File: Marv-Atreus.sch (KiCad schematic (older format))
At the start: 104 parts, among them SW1 SW_Push, U1 ATmega32U4-AU, U2 USBLC6-2SC6, Y1 Resonator_Small

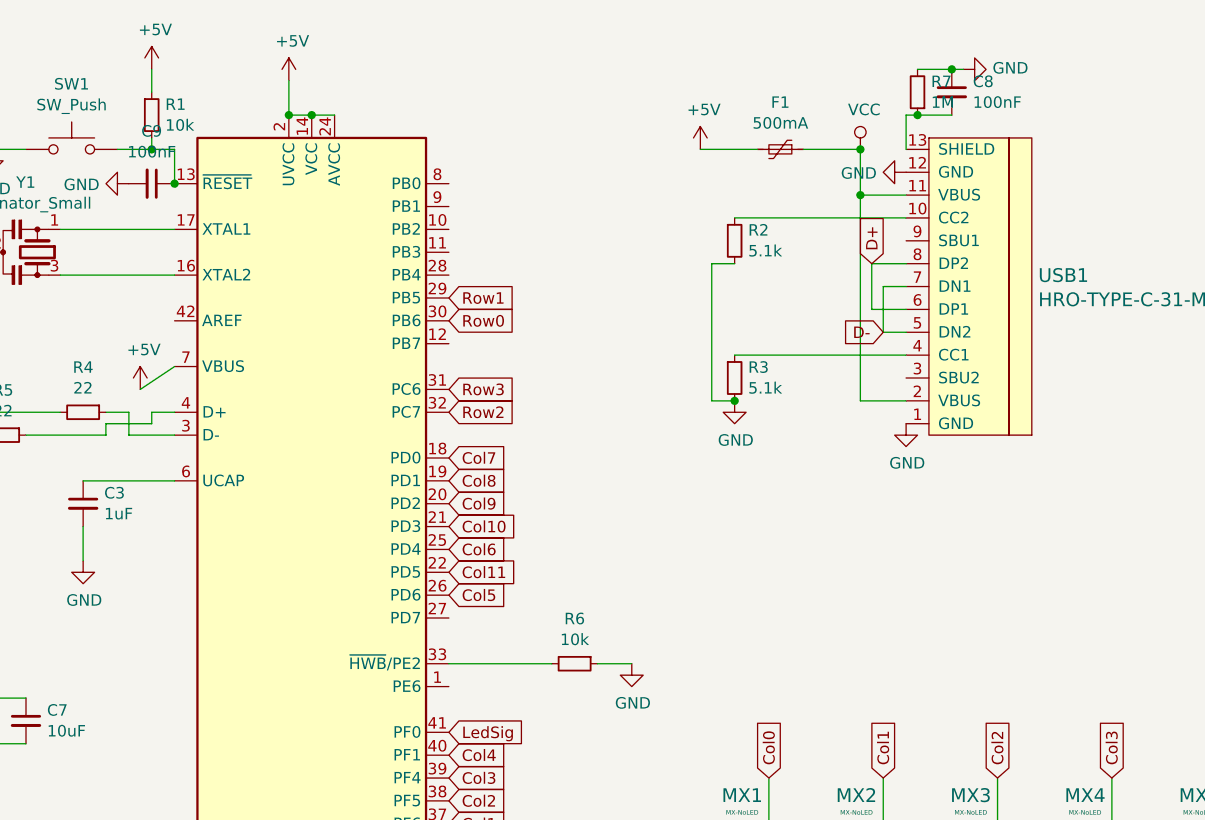
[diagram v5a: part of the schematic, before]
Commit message: Added ISP Connector
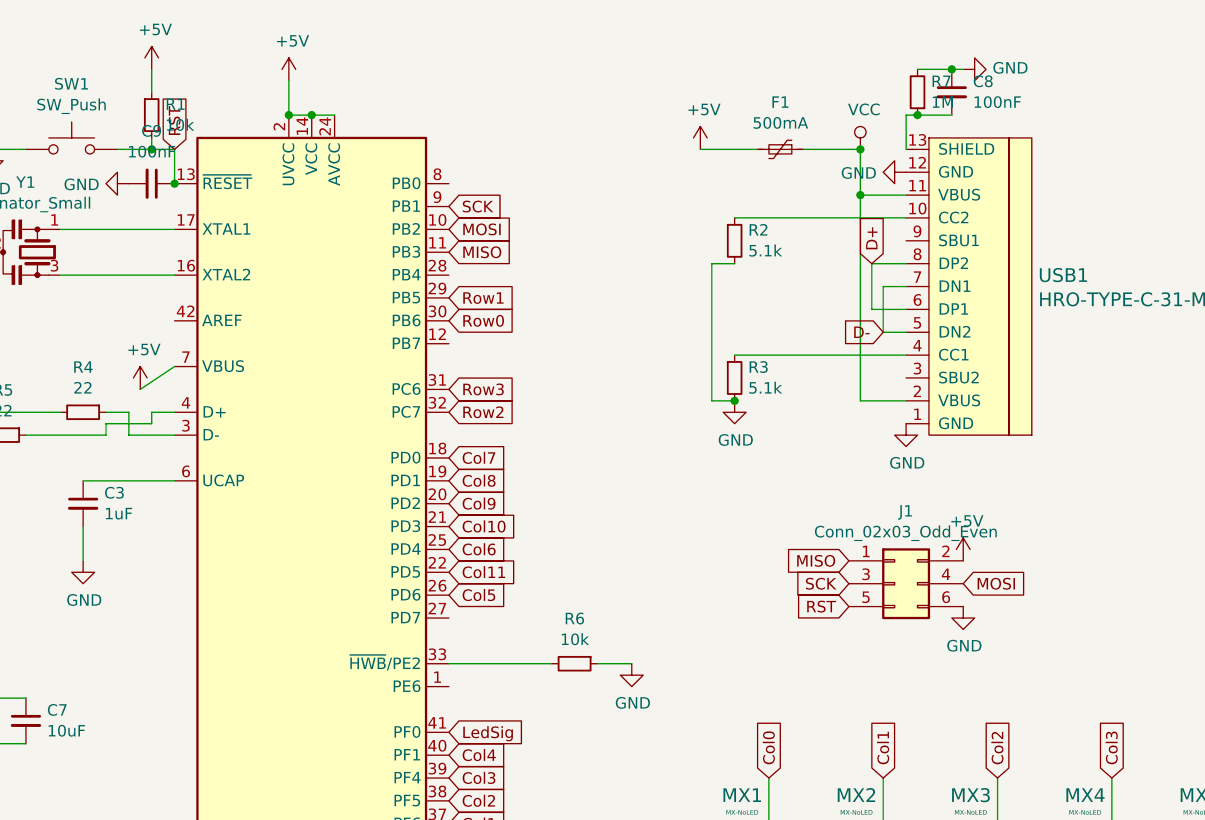
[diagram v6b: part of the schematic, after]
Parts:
- added J1: Conn_02x03_Odd_Even, Connector_PinHeader_2.54mm:PinHeader_2x03_P2.54mm_Vertical, symbol Connector_Generic:Conn_02x03_Odd_Even
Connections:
- net +5V: now also J1.2 (Pin_2)
- net GND: now also J1.6 (Pin_6)
- net MOSI: now reaches U1.10 (PB2)
- net MOSI: now also J1.4 (Pin_4)
- net MISO: now reaches U1.11 (PB3)
- net MISO: now also J1.1 (Pin_1)
- net RST: now reaches C9.1, R1.2, SW1.2, U1.13 (~RESET)
- net RST: now also J1.5 (Pin_5)
- net SCK: now reaches U1.9 (PB1)
- net SCK: now also J1.3 (Pin_3)
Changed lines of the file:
@@
 Wire Wire Line
 	2250 2300 2450 2300
+Text GLabel 5400 2850 0    50   Input ~ 0
+MISO
+$Comp
+L Connector_Generic:Conn_02x03_Odd_Even J1
+U 1 1 5EA26ACB
+P 5600 2950
+F 0 "J1" H 5650 3267 50  0000 C CNN
+F 1 "Conn_02x03_Odd_Even" H 5650 3176 50  0000 C CNN
+F 2 "Connector_PinHeader_2.54mm:PinHeader_2x03_P2.54mm_Vertical" H 5600 2950 50  0001 C CNN
+F 3 "~" H 5600 2950 50  0001 C CNN
+	1    5600 2950
+	1    0    0    -1
+$EndComp
+Text GLabel 5400 2950 0    50   Input ~ 0
+SCK
+Text GLabel 5400 3050 0    50   Input ~ 0
+RST
+Text GLabel 5900 2950 2    50   Input ~ 0
+MOSI
+$Comp
+L power:GND #PWR0120
+U 1 1 5EA59823
+P 5900 3050
+F 0 "#PWR0120" H 5900 2800 50  0001 C CNN
+F 1 "GND" H 5905 2877 50  0000 C CNN
+F 2 "" H 5900 3050 50  0001 C CNN
+F 3 "" H 5900 3050 50  0001 C CNN
+	1    5900 3050
+	1    0    0    -1
+$EndComp
+$Comp
+L power:+5V #PWR0121
+U 1 1 5EA5AFBB
+P 5900 2850
+F 0 "#PWR0121" H 5900 2700 50  0001 C CNN
+F 1 "+5V" H 5915 3023 50  0000 C CNN
+F 2 "" H 5900 2850 50  0001 C CNN
+F 3 "" H 5900 2850 50  0001 C CNN
+	1    5900 2850
+	1    0    0    -1
+$EndComp
+Text GLabel 3650 1300 2    50   Input ~ 0
+SCK
+Text GLabel 3650 1500 2    50   Input ~ 0
+MISO
+Text GLabel 3650 1400 2    50   Input ~ 0
+MOSI
+Text GLabel 2450 1050 1    50   Input ~ 0
+RST
 $EndSCHEMATC

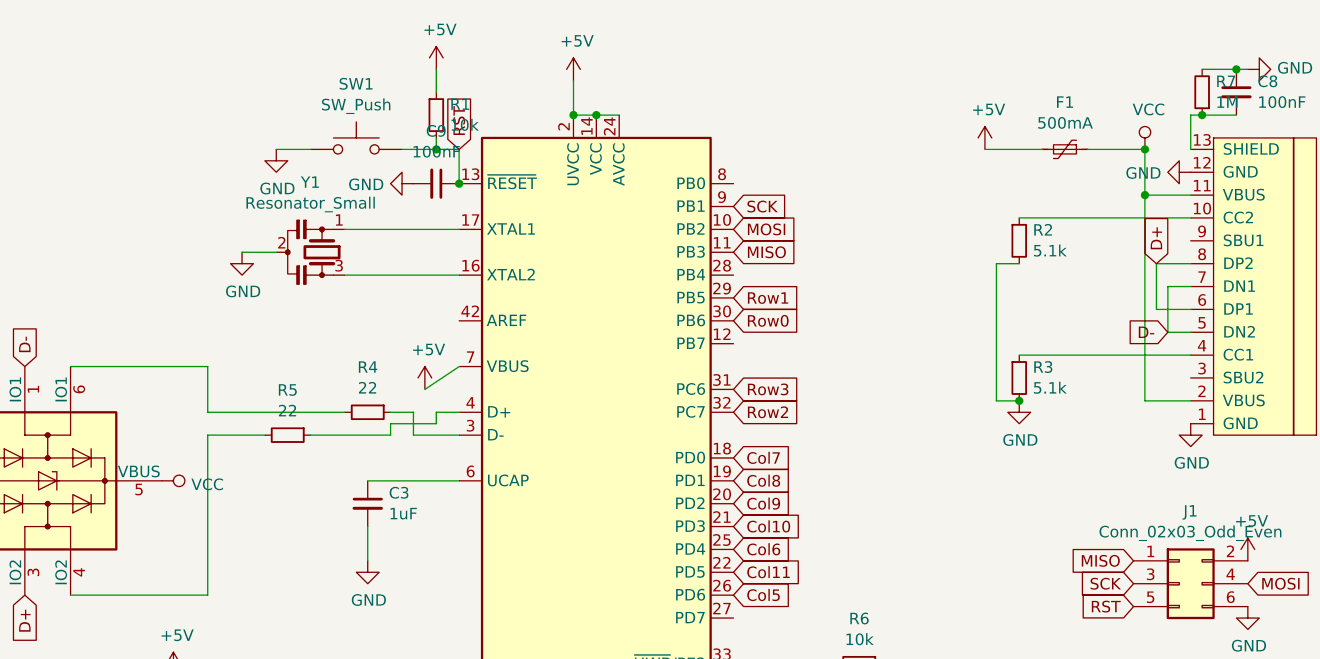
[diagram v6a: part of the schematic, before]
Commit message: Updates
- Added TVS diode to vbus
- Reinforced power lines
- More cleanup
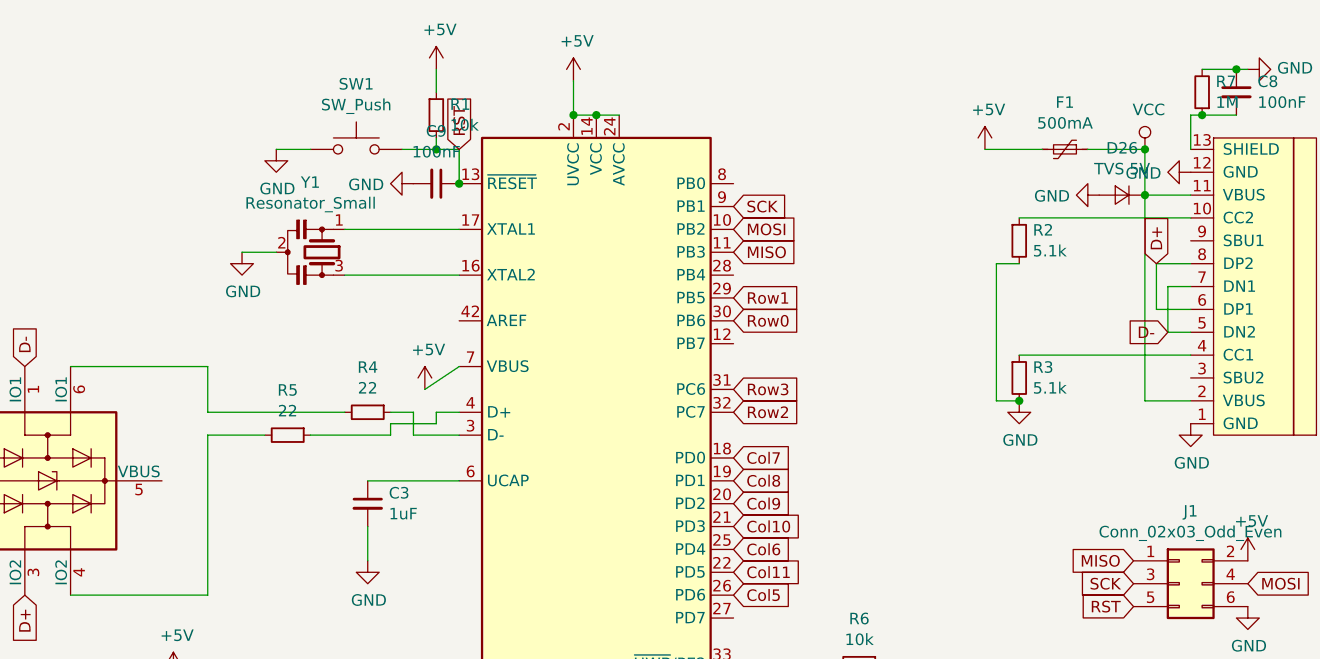
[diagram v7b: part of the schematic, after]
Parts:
- added D26: TVS 5V, Diode_SMD:D_SMB, symbol Device:D_Small
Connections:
- net GND: now also D26.2 (A)
- net VCC: now also D26.1 (K); no longer U2.5 (VBUS)
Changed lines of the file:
@@
 D-
-$Comp
-L power:VCC #PWR0118
-U 1 1 5EAC2933
-P 1150 2500
-F 0 "#PWR0118" H 1150 2350 50  0001 C CNN
-F 1 "VCC" V 1167 2628 50  0000 L CNN
-F 2 "" H 1150 2500 50  0001 C CNN
-F 3 "" H 1150 2500 50  0001 C CNN
-	1    1150 2500
-	0    1    1    0
-$EndComp
 $Comp
 L Device:Resonator_Small Y1
@@
 Text GLabel 2450 1050 1    50   Input ~ 0
 RST
+$Comp
+L Device:D_Small D26
+U 1 1 5EB4B2D8
+P 5350 1250
+F 0 "D26" H 5350 1045 50  0000 C CNN
+F 1 "TVS 5V" H 5350 1136 50  0000 C CNN
+F 2 "Diode_SMD:D_SMB" V 5350 1250 50  0001 C CNN
+F 3 "~" V 5350 1250 50  0001 C CNN
+	1    5350 1250
+	-1   0    0    1
+$EndComp
+$Comp
+L power:GND #PWR0118
+U 1 1 5EB4D10D
+P 5250 1250
+F 0 "#PWR0118" H 5250 1000 50  0001 C CNN
+F 1 "GND" V 5255 1122 50  0000 R CNN
+F 2 "" H 5250 1250 50  0001 C CNN
+F 3 "" H 5250 1250 50  0001 C CNN
+	1    5250 1250
+	0    1    1    0
+$EndComp
 $EndSCHEMATC
